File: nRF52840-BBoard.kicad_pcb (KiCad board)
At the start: 4 copper layers, 60 x 22.2 mm, 31 parts, among them J1 Conn_02x05_Odd_Even, J2 USB_C_Receptacle_USB2.0, J3 JST BATTERY INPUT, J4 Conn_01x20, J5 Conn_01x16, Q1 AO3407, SW1 SW_Push, U1 E73-2G4M08S1C-52840, U2 LTC4054, U3 AP2112K-3.3, Y1 32.768kHz

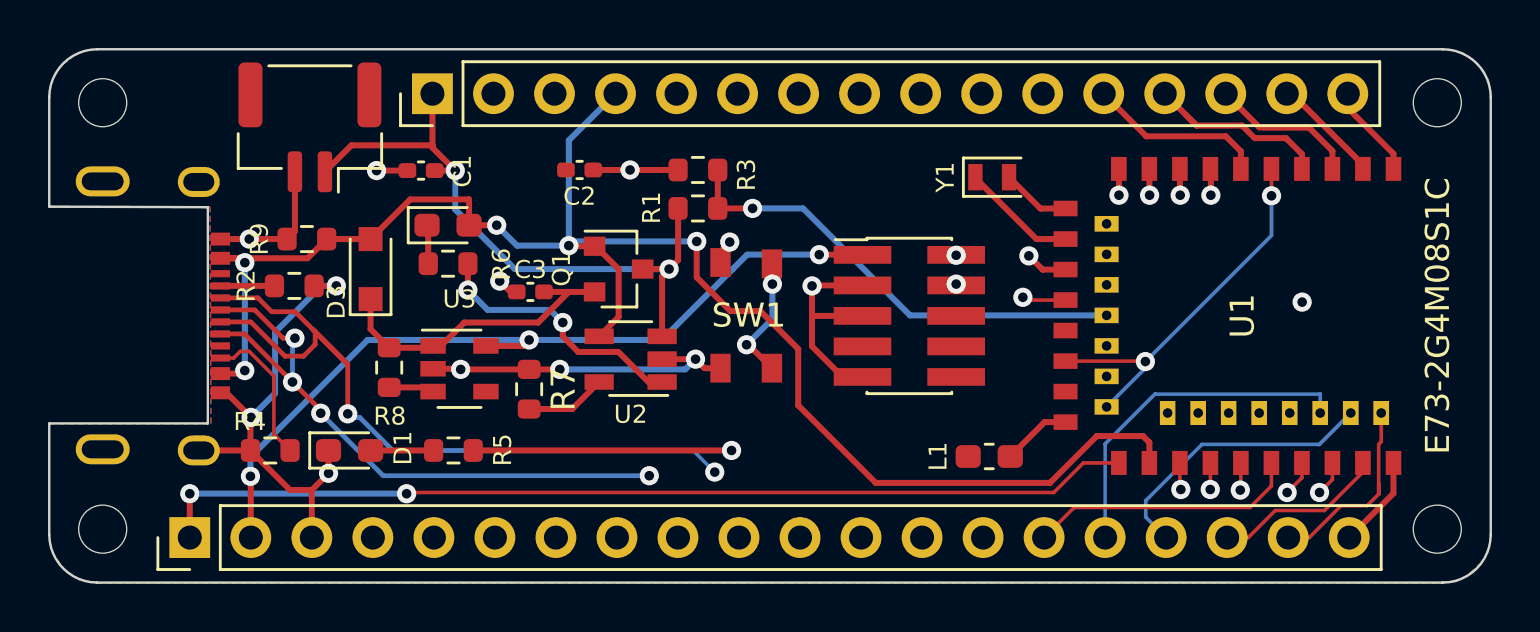
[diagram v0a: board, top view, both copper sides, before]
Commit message: added final version after testing
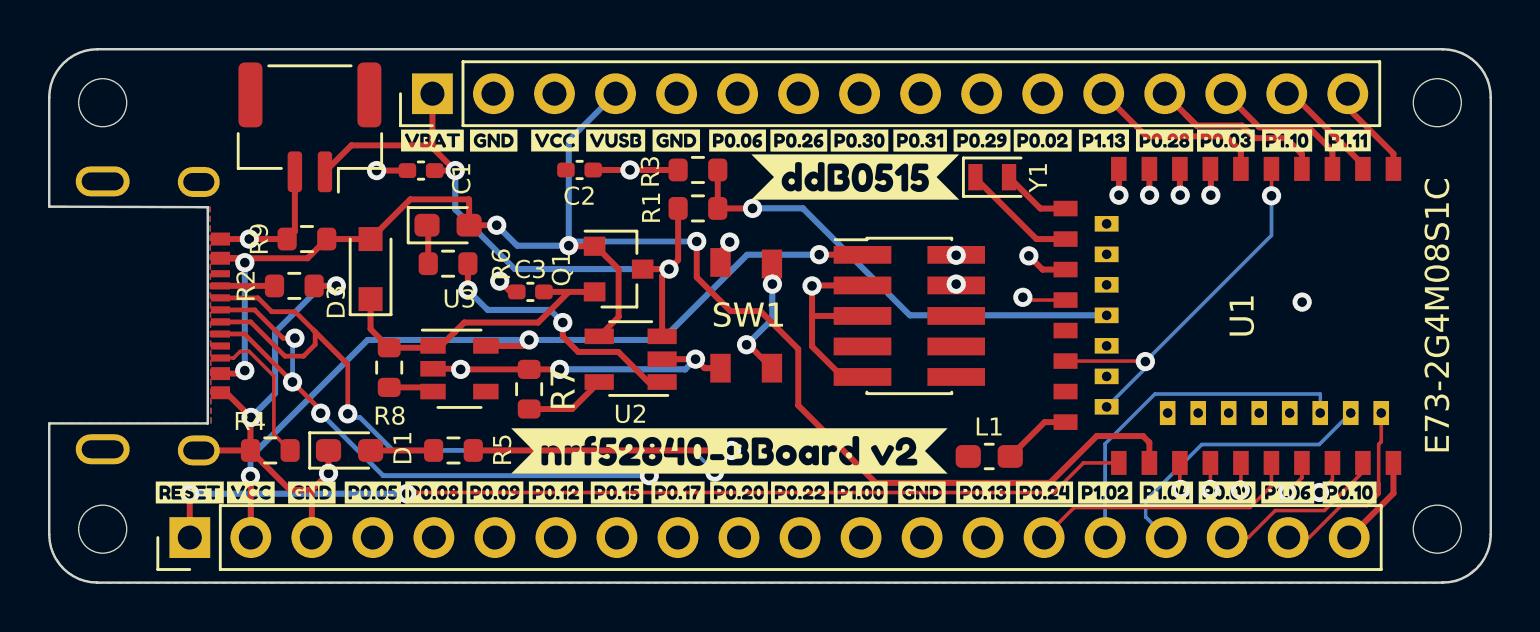
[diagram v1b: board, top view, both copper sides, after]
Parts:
- added svg2mod: G***, svg2mod, F.Cu at (121.3, 53.7)
- added svg2mod: G***, svg2mod, F.Cu at (103.6, 68.3)
- added svg2mod: G***, svg2mod, F.Cu at (85.8, 68.3)
- added svg2mod: G***, svg2mod, F.Cu at (98.5, 53.7)
- added svg2mod: G***, svg2mod, F.Cu at (108.6, 53.7)
- added svg2mod: G***, svg2mod, F.Cu at (116.3, 68.3)
- added svg2mod: G***, svg2mod, F.Cu at (129.0, 68.3)
- added svg2mod: G***, svg2mod, F.Cu at (113.8, 68.3)
- added svg2mod: G***, svg2mod, F.Cu at (126.5, 68.3)
- added svg2mod: G***, svg2mod, F.Cu at (98.5, 68.3)
- added svg2mod: G***, svg2mod, F.Cu at (80.8, 68.3)
- added svg2mod: G***, svg2mod, F.Cu at (90.9, 68.3)
- added svg2mod: G***, svg2mod, F.Cu at (108.5, 55.2)
- added svg2mod: G***, svg2mod, F.Cu at (118.8, 53.7)
- added svg2mod: G***, svg2mod, F.Cu at (116.2, 53.7)
- added svg2mod: G***, svg2mod, F.Cu at (123.9, 53.7)
- added svg2mod: G***, svg2mod, F.Cu at (126.4, 53.7)
- added svg2mod: G***, svg2mod, F.Cu at (111.2, 53.7)
- added svg2mod: G***, svg2mod, F.Cu at (113.7, 53.7)
- added svg2mod: G***, svg2mod, F.Cu at (101.0, 53.7)
- added svg2mod: G***, svg2mod, F.Cu at (90.8, 53.7)
- added svg2mod: G***, svg2mod, F.Cu at (106.1, 53.7)
- added svg2mod: G***, svg2mod, F.Cu at (93.5, 68.3)
- added svg2mod: G***, svg2mod, F.Cu at (118.8, 68.3)
- added svg2mod: G***, svg2mod, F.Cu at (101.1, 68.3)
- added svg2mod: G***, svg2mod, F.Cu at (93.4, 53.7)
- added svg2mod: G***, svg2mod, F.Cu at (123.9, 68.3)
- added svg2mod: G***, svg2mod, F.Cu at (128.9, 53.7)
- added svg2mod: G***, svg2mod, F.Cu at (121.4, 68.3)
- added svg2mod: G***, svg2mod, F.Cu at (96.0, 68.3)
- added svg2mod: G***, svg2mod, F.Cu at (108.7, 68.3)
- added svg2mod: G***, svg2mod, F.Cu at (103.2, 66.6)
- added svg2mod: G***, svg2mod, F.Cu at (83.3, 68.3)
- added svg2mod: G***, svg2mod, F.Cu at (103.5, 53.7)
- added svg2mod: G***, svg2mod, F.Cu at (88.4, 68.3)
- added svg2mod: G***, svg2mod, F.Cu at (96.0, 53.7)
- added svg2mod: G***, svg2mod, F.Cu at (106.2, 68.3)
- added svg2mod: G***, svg2mod, F.Cu at (111.2, 68.3)
